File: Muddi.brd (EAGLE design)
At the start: 106.3 x 85 mm, 13 parts, among them IC1 7805TV, J1 DCJ0202

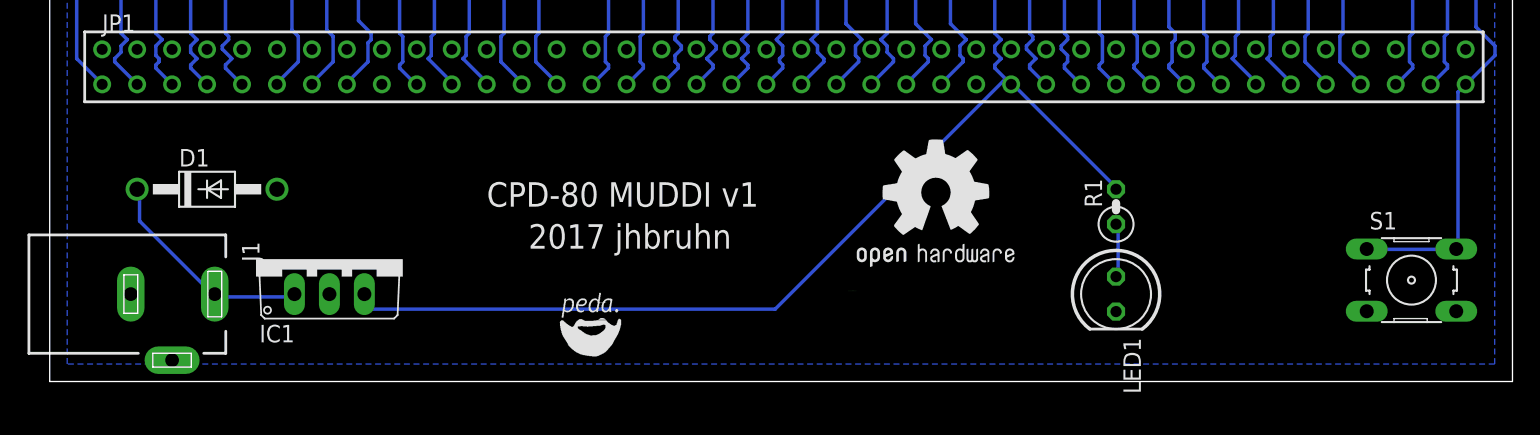
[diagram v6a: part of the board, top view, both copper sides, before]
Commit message: Make Top Plane a VCC Plane instead of Ground, add Holes
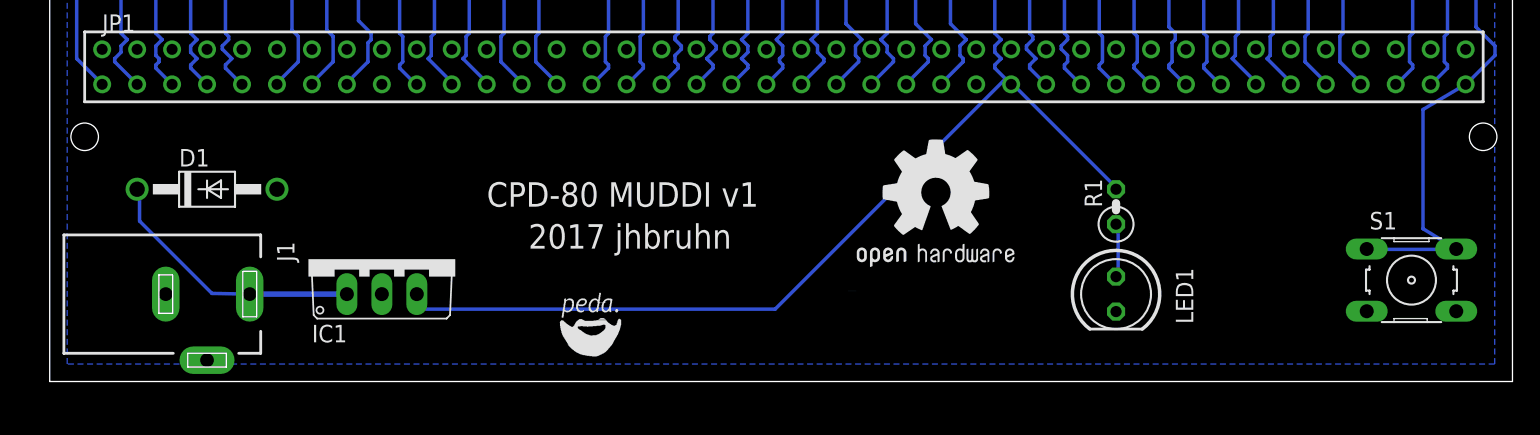
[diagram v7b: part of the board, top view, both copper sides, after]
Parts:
- moved IC1 3.81 mm to (22.9, 8.89)
- moved J1 2.54 mm to (10.2, 6.35)
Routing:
- net VCC: track 131.6 -> 127.9 mm
- net N$26: track 16.2 -> 19.7 mm
- net N$40: track 88.7 -> 91.6 mm
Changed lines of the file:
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@@
 <rectangle x1="38.6461" y1="6.4135" x2="38.7731" y2="6.4389" layer="21"/>
 <text x="48.26" y="11.43" size="1.778" layer="21" font="fixed" rot="R180">2017 jhbruhn</text>
+<hole x="1.27" y="17.78" drill="2"/>
+<hole x="102.87" y="17.78" drill="2"/>
 </plain>
 <attributes>
@@
 <attribute name="OC_FARNELL" value="1126305" x="10.16" y="13.97" size="1.778" layer="27" display="off"/>
 </element>
-<element name="J1" library="con-jack" package="DCJ0202" value="DCJ0202" x="7.62" y="6.35" rot="R270">
-<attribute name="MPN" value="" x="7.62" y="6.35" size="1.778" layer="27" rot="R270" display="off"/>
-<attribute name="OC_NEWARK" value="unknown" x="7.62" y="6.35" size="1.778" layer="27" rot="R270" display="off"/>
-<attribute name="MF" value="" x="7.62" y="6.35" size="1.778" layer="27" rot="R270" display="off"/>
-<attribute name="OC_FARNELL" value="unknown" x="7.62" y="6.35" size="1.778" layer="27" rot="R270" display="off"/>
+<element name="J1" library="con-jack" package="DCJ0202" value="DCJ0202" x="10.16" y="6.35" rot="R270">
+<attribute name="MPN" value="" x="10.16" y="6.35" size="1.778" layer="27" rot="R270" display="off"/>
+<attribute name="OC_NEWARK" value="unknown" x="10.16" y="6.35" size="1.778" layer="27" rot="R270" display="off"/>
+<attribute name="MF" value="" x="10.16" y="6.35" size="1.778" layer="27" rot="R270" display="off"/>
+<attribute name="OC_FARNELL" value="unknown" x="10.16" y="6.35" size="1.778" layer="27" rot="R270" display="off"/>
 </element>
 <element name="JP1" library="jean" package="57102-F08-25" value="" x="11.43" y="22.86"/>
@@
 <attribute name="MF" value="OMRON ELECTRONIC COMPONENTS" x="97.663" y="7.366" size="1.778" layer="27" display="off"/>
 </element>
-<element name="LED1" library="led" package="LED5MM" value="BW" x="76.2" y="6.35" rot="R270"/>
+<element name="LED1" library="led" package="LED5MM" value="BW" x="76.2" y="6.35" smashed="yes" rot="R270">
+<attribute name="NAME" x="80.5434" y="8.255" size="1.27" layer="25" ratio="10" rot="R270"/>
+<attribute name="VALUE" x="70.5866" y="6.9596" size="1.27" layer="27" ratio="10" rot="R270"/>
+</element>
 <element name="R1" library="resistor" package="0207/2V" value="560" x="76.2" y="12.7" rot="R90"/>
 <element name="U$1" library="bfl" package="OSHW1" value="" x="56.7436" y="6.604"/>
-<element name="IC1" library="linear" package="TO220V" value="7805TV" x="19.05" y="8.89"/>
+<element name="IC1" library="linear" package="TO220V" value="7805TV" x="22.86" y="8.89"/>
 </elements>
 <signals>
@@
 <wire x1="94.4118" y1="9.6012" x2="94.4118" y2="9.6266" width="0.254" layer="16"/>
 <wire x1="100.8126" y1="9.6012" x2="100.9142" y2="9.6266" width="0.254" layer="16"/>
-<wire x1="101.0412" y1="21.0312" x2="101.0412" y2="9.8298" width="0.254" layer="16"/>
-<wire x1="101.6" y1="21.59" x2="101.0412" y2="21.0312" width="0.254" layer="16"/>
-<wire x1="101.0412" y1="9.8298" x2="100.9142" y2="9.6266" width="0.254" layer="16"/>
+<wire x1="98.5012" y1="19.7612" x2="98.5012" y2="11.0998" width="0.254" layer="16"/>
+<wire x1="101.6" y1="21.59" x2="98.5012" y2="19.7612" width="0.254" layer="16"/>
+<wire x1="98.5012" y1="11.0998" x2="100.9142" y2="9.6266" width="0.254" layer="16"/>
 </signal>
 <signal name="N$41">
@@
 <wire x1="76.1238" y1="14.1732" x2="76.2" y2="13.97" width="0.254" layer="16"/>
 <wire x1="68.58" y1="21.717" x2="68.58" y2="21.59" width="0.254" layer="16"/>
-<wire x1="51.435" y1="5.2578" x2="21.717" y2="5.2578" width="0.254" layer="16"/>
+<wire x1="51.435" y1="5.2578" x2="25.4" y2="5.2578" width="0.254" layer="16"/>
 <wire x1="68.1228" y1="21.9456" x2="51.435" y2="5.2578" width="0.254" layer="16"/>
-<wire x1="21.717" y1="5.2578" x2="21.59" y2="6.35" width="0.254" layer="16"/>
+<wire x1="25.4" y1="5.2578" x2="25.4" y2="6.35" width="0.254" layer="16"/>
 <wire x1="68.1228" y1="21.9456" x2="68.58" y2="21.59" width="0.254" layer="16"/>
 </signal>
@@
 <contactref element="IC1" pad="1"/>
 <contactref element="D1" pad="C"/>
-<wire x1="11.6586" y1="6.1468" x2="16.4592" y2="6.1468" width="0.254" layer="16"/>
-<wire x1="10.7442" y1="6.1722" x2="11.6586" y2="6.1468" width="0.254" layer="16"/>
-<wire x1="16.4592" y1="6.1468" x2="16.51" y2="6.35" width="0.254" layer="16"/>
-<wire x1="10.7442" y1="6.1722" x2="10.72" y2="6.35" width="0.254" layer="16"/>
 <wire x1="5.2578" y1="11.6586" x2="5.2578" y2="13.9446" width="0.254" layer="16"/>
 <wire x1="10.5156" y1="6.4008" x2="5.2578" y2="11.6586" width="0.254" layer="16"/>
 <wire x1="5.2578" y1="13.9446" x2="5.08" y2="13.97" width="0.254" layer="16"/>
-<wire x1="10.5156" y1="6.4008" x2="10.72" y2="6.35" width="0.254" layer="16"/>
+<wire x1="10.5156" y1="6.4008" x2="13.26" y2="6.35" width="0.254" layer="16"/>
+<wire x1="13.26" y1="6.35" x2="20.32" y2="6.35" width="0.4064" layer="16"/>
 </signal>
 </signals>

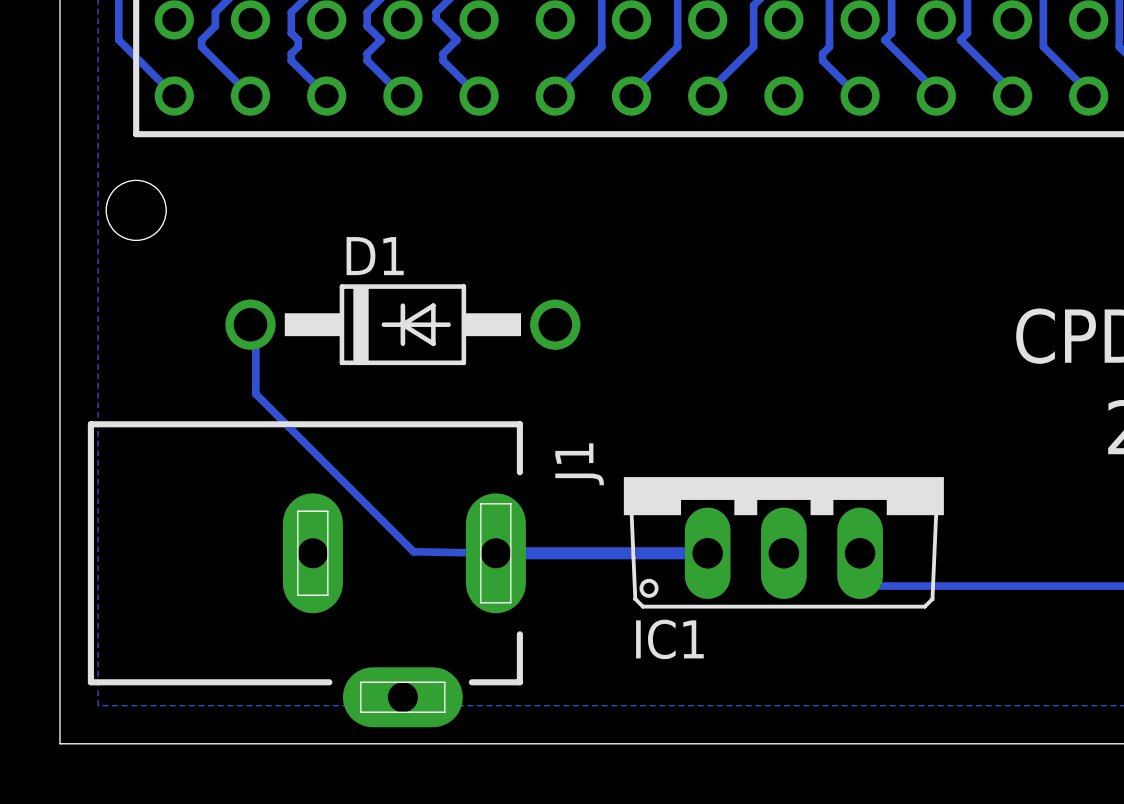
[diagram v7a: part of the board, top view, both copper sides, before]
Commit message: Correctly wire the Enable on SerialCF 74138
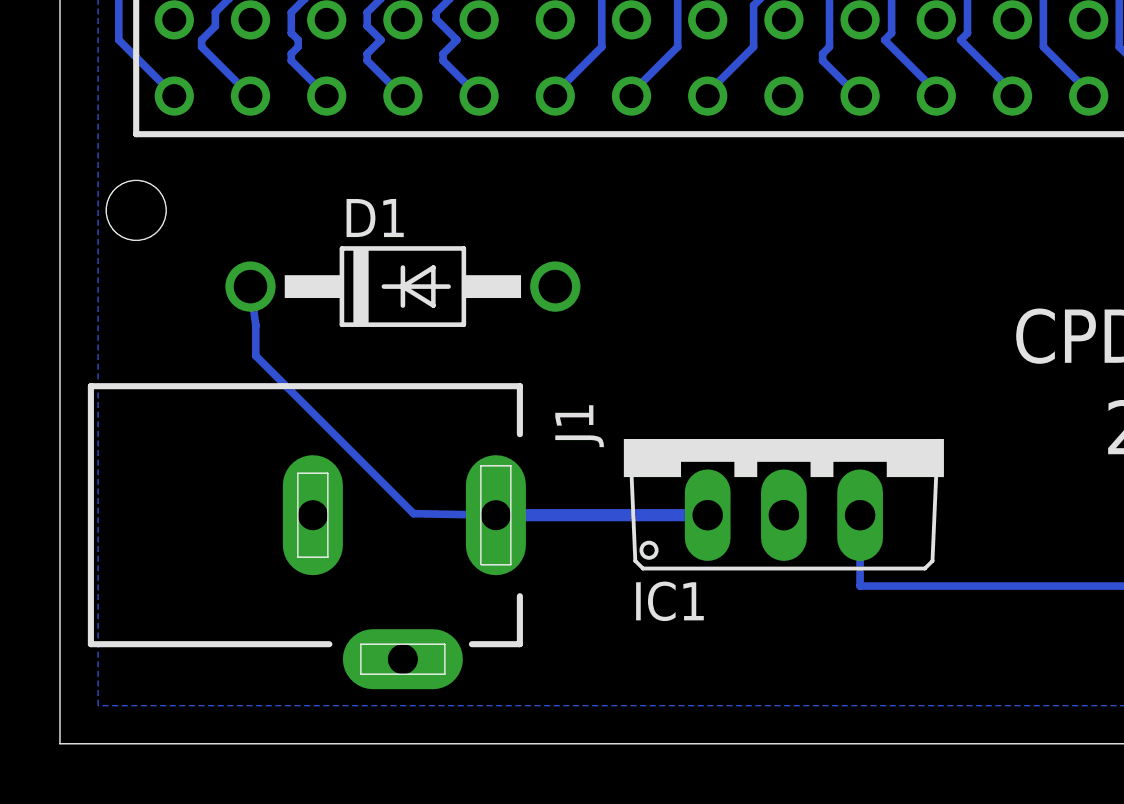
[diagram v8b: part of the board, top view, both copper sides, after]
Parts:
- moved J1 1.27 mm to (10.2, 7.62)
- moved D1 1.27 mm to (10.2, 15.2)
- moved IC1 1.27 mm to (22.9, 10.2)
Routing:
- net VCC: track 127.9 -> 129.2 mm
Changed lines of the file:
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@@
 </autorouter>
 <elements>
-<element name="D1" library="diode" package="DO41-10" value="1N4942" x="10.16" y="13.97">
-<attribute name="MPN" value="1N4935G" x="10.16" y="13.97" size="1.778" layer="27" display="off"/>
-<attribute name="MF" value="ON SEMICONDUCTOR" x="10.16" y="13.97" size="1.778" layer="27" display="off"/>
-<attribute name="OC_FARNELL" value="1126305" x="10.16" y="13.97" size="1.778" layer="27" display="off"/>
+<element name="D1" library="diode" package="DO41-10" value="1N4942" x="10.16" y="15.24">
+<attribute name="MPN" value="1N4935G" x="10.16" y="15.24" size="1.778" layer="27" display="off"/>
+<attribute name="MF" value="ON SEMICONDUCTOR" x="10.16" y="15.24" size="1.778" layer="27" display="off"/>
+<attribute name="OC_FARNELL" value="1126305" x="10.16" y="15.24" size="1.778" layer="27" display="off"/>
 </element>
-<element name="J1" library="con-jack" package="DCJ0202" value="DCJ0202" x="10.16" y="6.35" rot="R270">
-<attribute name="MPN" value="" x="10.16" y="6.35" size="1.778" layer="27" rot="R270" display="off"/>
-<attribute name="OC_NEWARK" value="unknown" x="10.16" y="6.35" size="1.778" layer="27" rot="R270" display="off"/>
-<attribute name="MF" value="" x="10.16" y="6.35" size="1.778" layer="27" rot="R270" display="off"/>
-<attribute name="OC_FARNELL" value="unknown" x="10.16" y="6.35" size="1.778" layer="27" rot="R270" display="off"/>
+<element name="J1" library="con-jack" package="DCJ0202" value="DCJ0202" x="10.16" y="7.62" rot="R270">
+<attribute name="MPN" value="" x="10.16" y="7.62" size="1.778" layer="27" rot="R270" display="off"/>
+<attribute name="OC_NEWARK" value="unknown" x="10.16" y="7.62" size="1.778" layer="27" rot="R270" display="off"/>
+<attribute name="MF" value="" x="10.16" y="7.62" size="1.778" layer="27" rot="R270" display="off"/>
+<attribute name="OC_FARNELL" value="unknown" x="10.16" y="7.62" size="1.778" layer="27" rot="R270" display="off"/>
 </element>
 <element name="JP1" library="jean" package="57102-F08-25" value="" x="11.43" y="22.86"/>
@@
 <element name="R1" library="resistor" package="0207/2V" value="560" x="76.2" y="12.7" rot="R90"/>
 <element name="U$1" library="bfl" package="OSHW1" value="" x="56.7436" y="6.604"/>
-<element name="IC1" library="linear" package="TO220V" value="7805TV" x="22.86" y="8.89"/>
+<element name="IC1" library="linear" package="TO220V" value="7805TV" x="22.86" y="10.16"/>
 </elements>
 <signals>
@@
 <wire x1="51.435" y1="5.2578" x2="25.4" y2="5.2578" width="0.254" layer="16"/>
 <wire x1="68.1228" y1="21.9456" x2="51.435" y2="5.2578" width="0.254" layer="16"/>
-<wire x1="25.4" y1="5.2578" x2="25.4" y2="6.35" width="0.254" layer="16"/>
+<wire x1="25.4" y1="5.2578" x2="25.4" y2="7.62" width="0.254" layer="16"/>
 <wire x1="68.1228" y1="21.9456" x2="68.58" y2="21.59" width="0.254" layer="16"/>
 </signal>
@@
 <contactref element="IC1" pad="1"/>
 <contactref element="D1" pad="C"/>
-<wire x1="5.2578" y1="11.6586" x2="5.2578" y2="13.9446" width="0.254" layer="16"/>
-<wire x1="10.5156" y1="6.4008" x2="5.2578" y2="11.6586" width="0.254" layer="16"/>
-<wire x1="5.2578" y1="13.9446" x2="5.08" y2="13.97" width="0.254" layer="16"/>
-<wire x1="10.5156" y1="6.4008" x2="13.26" y2="6.35" width="0.254" layer="16"/>
-<wire x1="13.26" y1="6.35" x2="20.32" y2="6.35" width="0.4064" layer="16"/>
+<wire x1="5.2578" y1="12.9286" x2="5.2578" y2="13.9446" width="0.254" layer="16"/>
+<wire x1="10.5156" y1="7.6708" x2="5.2578" y2="12.9286" width="0.254" layer="16"/>
+<wire x1="5.2578" y1="13.9446" x2="5.08" y2="15.24" width="0.254" layer="16"/>
+<wire x1="10.5156" y1="7.6708" x2="13.26" y2="7.62" width="0.254" layer="16"/>
+<wire x1="13.26" y1="7.62" x2="20.32" y2="7.62" width="0.4064" layer="16"/>
 </signal>
 </signals>
